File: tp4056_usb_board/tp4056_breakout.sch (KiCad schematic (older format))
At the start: 15 parts, among them J1 USB_OTG, J2 CONN_02X04, J3 DW01, J4 8205A, U1 TP4056_BREAKOUT

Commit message: Started the charging+UART breakout
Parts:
- C1, C2: footprint Capacitors_SMD:C_0805 -> Capacitors_SMD:C_0603
- D1, D2: footprint Diodes_SMD:D_0805 -> Diodes_SMD:D_0603
- J1: footprint (none) -> footprints:MICROUSB_SIMPLE
- R1, R2, R3, R4, R5: footprint Resistors_SMD:R_0805 -> Resistors_SMD:R_0603
- U1: footprint (none) -> tp4056_usb_board:TP4056_BREAKOUT
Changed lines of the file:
@@
 LIBS:valves
 LIBS:tp4056_breakout
+LIBS:tp4056_breakout-cache
 EELAYER 25 0
 EELAYER END
@@
 F 0 "C2" H 5775 2650 50  0000 L CNN
 F 1 "C" H 5775 2450 50  0000 L CNN
-F 2 "Capacitors_SMD:C_0805" H 5788 2400 50  0001 C CNN
+F 2 "Capacitors_SMD:C_0603" H 5788 2400 50  0001 C CNN
 F 3 "" H 5750 2550 50  0001 C CNN
 	1    5750 2550
@@
 F 0 "J1" H 3400 3000 50  0000 L CNN
 F 1 "USB_OTG" H 3400 2900 50  0000 L CNN
-F 2 "" H 3750 2500 50  0001 C CNN
+F 2 "footprints:MICROUSB_SIMPLE" H 3750 2500 50  0001 C CNN
 F 3 "" H 3750 2500 50  0001 C CNN
 	1    3600 2550
@@
 F 0 "R4" V 6480 2350 50  0000 C CNN
 F 1 "R" V 6400 2350 50  0000 C CNN
-F 2 "Resistors_SMD:R_0805" V 6330 2350 50  0001 C CNN
+F 2 "Resistors_SMD:R_0603" V 6330 2350 50  0001 C CNN
 F 3 "" H 6400 2350 50  0001 C CNN
 	1    6400 2350
@@
 F 0 "D2" H 5850 3900 50  0000 C CNN
 F 1 "LED" H 5850 3700 50  0000 C CNN
-F 2 "Diodes_SMD:D_0805" H 5850 3800 50  0001 C CNN
+F 2 "Diodes_SMD:D_0603" H 5850 3800 50  0001 C CNN
 F 3 "" H 5850 3800 50  0001 C CNN
 	1    5850 3800
@@
 F 0 "R3" V 5630 3800 50  0000 C CNN
 F 1 "R" V 5550 3800 50  0000 C CNN
-F 2 "Resistors_SMD:R_0805" V 5480 3800 50  0001 C CNN
+F 2 "Resistors_SMD:R_0603" V 5480 3800 50  0001 C CNN
 F 3 "" H 5550 3800 50  0001 C CNN
 	1    5550 3800
@@
 F 0 "D1" H 4450 4000 50  0000 C CNN
 F 1 "LED" H 4450 3800 50  0000 C CNN
-F 2 "Diodes_SMD:D_0805" H 4450 3900 50  0001 C CNN
+F 2 "Diodes_SMD:D_0603" H 4450 3900 50  0001 C CNN
 F 3 "" H 4450 3900 50  0001 C CNN
 	1    4450 3900
@@
 F 0 "R1" V 4650 3900 50  0000 C CNN
 F 1 "R" V 4750 3900 50  0000 C CNN
-F 2 "Resistors_SMD:R_0805" V 4680 3900 50  0001 C CNN
+F 2 "Resistors_SMD:R_0603" V 4680 3900 50  0001 C CNN
 F 3 "" H 4750 3900 50  0001 C CNN
 	1    4750 3900
@@
 $EndComp
 $Comp
-L VSS #PWR15
+L VSS #PWR01
 U 1 1 595C1537
 P 5750 2400
-F 0 "#PWR15" H 5750 2250 50  0001 C CNN
+F 0 "#PWR01" H 5750 2250 50  0001 C CNN
 F 1 "VSS" V 5750 2600 50  0000 C CNN
 F 2 "" H 5750 2400 50  0001 C CNN
@@
 NoConn ~ 3900 2750
 $Comp
-L GND #PWR1
+L GND #PWR02
 U 1 1 595C168E
 P 3500 2950
-F 0 "#PWR1" H 3500 2700 50  0001 C CNN
+F 0 "#PWR02" H 3500 2700 50  0001 C CNN
 F 1 "GND" H 3500 2800 50  0000 C CNN
 F 2 "" H 3500 2950 50  0001 C CNN
@@
 $EndComp
 $Comp
-L GND #PWR2
+L GND #PWR03
 U 1 1 595C16C7
 P 3600 2950
-F 0 "#PWR2" H 3600 2700 50  0001 C CNN
+F 0 "#PWR03" H 3600 2700 50  0001 C CNN
 F 1 "GND" H 3600 2800 50  0000 C CNN
 F 2 "" H 3600 2950 50  0001 C CNN
@@
 F 0 "C1" H 4825 3550 50  0000 L CNN
 F 1 "C" H 4825 3350 50  0000 L CNN
-F 2 "Capacitors_SMD:C_0805" H 4838 3300 50  0001 C CNN
+F 2 "Capacitors_SMD:C_0603" H 4838 3300 50  0001 C CNN
 F 3 "" H 4800 3450 50  0001 C CNN
 	1    4800 3450
@@
 F 0 "R2" V 5580 3450 50  0000 C CNN
 F 1 "R" V 5500 3450 50  0000 C CNN
-F 2 "Resistors_SMD:R_0805" V 5430 3450 50  0001 C CNN
+F 2 "Resistors_SMD:R_0603" V 5430 3450 50  0001 C CNN
 F 3 "" H 5500 3450 50  0001 C CNN
 	1    5500 3450
@@
 $EndComp
 $Comp
-L GND #PWR14
+L GND #PWR04
 U 1 1 595C1A34
 P 5500 3300
-F 0 "#PWR14" H 5500 3050 50  0001 C CNN
+F 0 "#PWR04" H 5500 3050 50  0001 C CNN
 F 1 "GND" H 5500 3150 50  0000 C CNN
 F 2 "" H 5500 3300 50  0001 C CNN
@@
 $EndComp
 $Comp
-L GND #PWR8
+L GND #PWR05
 U 1 1 595C1C7D
 P 4900 3700
-F 0 "#PWR8" H 4900 3450 50  0001 C CNN
+F 0 "#PWR05" H 4900 3450 50  0001 C CNN
 F 1 "GND" V 4850 3500 50  0000 C CNN
 F 2 "" H 4900 3700 50  0001 C CNN
@@
 $EndComp
 $Comp
-L +5V #PWR3
+L +5V #PWR06
 U 1 1 595C216B
 P 3900 2350
-F 0 "#PWR3" H 3900 2200 50  0001 C CNN
+F 0 "#PWR06" H 3900 2200 50  0001 C CNN
 F 1 "+5V" H 3900 2490 50  0000 C CNN
 F 2 "" H 3900 2350 50  0001 C CNN
@@
 $EndComp
 $Comp
-L +5V #PWR17
+L +5V #PWR07
 U 1 1 595C21FD
 P 6000 3800
-F 0 "#PWR17" H 6000 3650 50  0001 C CNN
+F 0 "#PWR07" H 6000 3650 50  0001 C CNN
 F 1 "+5V" H 6000 3940 50  0000 C CNN
 F 2 "" H 6000 3800 50  0001 C CNN
@@
 $EndComp
 $Comp
-L +5V #PWR12
+L +5V #PWR08
 U 1 1 595C2374
 P 5400 3700
-F 0 "#PWR12" H 5400 3550 50  0001 C CNN
+F 0 "#PWR08" H 5400 3550 50  0001 C CNN
 F 1 "+5V" V 5400 3900 50  0000 C CNN
 F 2 "" H 5400 3700 50  0001 C CNN
@@
 $EndComp
 $Comp
-L +5V #PWR7
+L +5V #PWR09
 U 1 1 595C23EE
 P 4800 3300
-F 0 "#PWR7" H 4800 3150 50  0001 C CNN
+F 0 "#PWR09" H 4800 3150 50  0001 C CNN
 F 1 "+5V" H 4800 3440 50  0000 C CNN
 F 2 "" H 4800 3300 50  0001 C CNN
@@
 $EndComp
 $Comp
-L +5V #PWR13
+L +5V #PWR010
 U 1 1 595C2423
 P 5400 3900
-F 0 "#PWR13" H 5400 3750 50  0001 C CNN
+F 0 "#PWR010" H 5400 3750 50  0001 C CNN
 F 1 "+5V" V 5500 4050 50  0000 C CNN
 F 2 "" H 5400 3900 50  0001 C CNN
@@
 $EndComp
 $Comp
-L +5V #PWR4
+L +5V #PWR011
 U 1 1 595C271A
 P 4300 3900
-F 0 "#PWR4" H 4300 3750 50  0001 C CNN
+F 0 "#PWR011" H 4300 3750 50  0001 C CNN
 F 1 "+5V" H 4300 4040 50  0000 C CNN
 F 2 "" H 4300 3900 50  0001 C CNN
@@
 $EndComp
 $Comp
-L GND #PWR16
+L GND #PWR012
 U 1 1 595C274F
 P 5750 2700
-F 0 "#PWR16" H 5750 2450 50  0001 C CNN
+F 0 "#PWR012" H 5750 2450 50  0001 C CNN
 F 1 "GND" V 5700 2500 50  0000 C CNN
 F 2 "" H 5750 2700 50  0001 C CNN
@@
 $EndComp
 $Comp
-L VSS #PWR9
+L VSS #PWR013
 U 1 1 595C2784
 P 4900 3800
-F 0 "#PWR9" H 4900 3650 50  0001 C CNN
+F 0 "#PWR013" H 4900 3650 50  0001 C CNN
 F 1 "VSS" V 4900 4000 50  0000 C CNN
 F 2 "" H 4900 3800 50  0001 C CNN
@@
 $EndComp
 $Comp
-L VSS #PWR18
+L VSS #PWR014
 U 1 1 595C27B9
 P 6400 2200
-F 0 "#PWR18" H 6400 2050 50  0001 C CNN
+F 0 "#PWR014" H 6400 2050 50  0001 C CNN
 F 1 "VSS" V 6400 2400 50  0000 C CNN
 F 2 "" H 6400 2200 50  0001 C CNN
@@
 $EndComp
 $Comp
-L GND #PWR19
+L GND #PWR015
 U 1 1 595C27EE
 P 7350 2900
-F 0 "#PWR19" H 7350 2650 50  0001 C CNN
+F 0 "#PWR015" H 7350 2650 50  0001 C CNN
 F 1 "GND" H 7350 2750 50  0000 C CNN
 F 2 "" H 7350 2900 50  0001 C CNN
@@
 	6950 3200 6950 3350
 $Comp
-L GND #PWR20
+L GND #PWR016
 U 1 1 595C2A57
 P 6950 3900
-F 0 "#PWR20" H 6950 3650 50  0001 C CNN
+F 0 "#PWR016" H 6950 3650 50  0001 C CNN
 F 1 "GND" V 6900 3700 50  0000 C CNN
 F 2 "" H 6950 3900 50  0001 C CNN
@@
 F 0 "U1" H 4600 2300 60  0000 C CNN
 F 1 "TP4056_BREAKOUT" H 4900 2800 60  0000 C CNN
-F 2 "" H 4800 2550 60  0001 C CNN
+F 2 "tp4056_usb_board:TP4056_BREAKOUT" H 4800 2550 60  0001 C CNN
 F 3 "" H 4800 2550 60  0001 C CNN
 	1    4800 2550
@@
 $EndComp
 $Comp
-L +5V #PWR10
+L +5V #PWR017
 U 1 1 595C2D30
 P 5250 2500
-F 0 "#PWR10" H 5250 2350 50  0001 C CNN
+F 0 "#PWR017" H 5250 2350 50  0001 C CNN
 F 1 "+5V" H 5250 2640 50  0000 C CNN
 F 2 "" H 5250 2500 50  0001 C CNN
@@
 $EndComp
 $Comp
-L GND #PWR11
+L GND #PWR018
 U 1 1 595C2D68
 P 5250 2600
-F 0 "#PWR11" H 5250 2350 50  0001 C CNN
+F 0 "#PWR018" H 5250 2350 50  0001 C CNN
 F 1 "GND" V 5200 2400 50  0000 C CNN
 F 2 "" H 5250 2600 50  0001 C CNN
@@
 $EndComp
 $Comp
-L GND #PWR6
+L GND #PWR019
 U 1 1 595C2DA0
 P 4350 2700
-F 0 "#PWR6" H 4350 2450 50  0001 C CNN
+F 0 "#PWR019" H 4350 2450 50  0001 C CNN
 F 1 "GND" V 4300 2500 50  0000 C CNN
 F 2 "" H 4350 2700 50  0001 C CNN
@@
 	4350 2400 4350 2500
 $Comp
-L VSS #PWR5
+L VSS #PWR020
 U 1 1 595C2E3E
 P 4350 2400
-F 0 "#PWR5" H 4350 2250 50  0001 C CNN
+F 0 "#PWR020" H 4350 2250 50  0001 C CNN
 F 1 "VSS" V 4350 2600 50  0000 C CNN
 F 2 "" H 4350 2400 50  0001 C CNN
@@
 F 0 "R5" V 7280 2900 50  0000 C CNN
 F 1 "R" V 7200 2900 50  0000 C CNN
-F 2 "Resistors_SMD:R_0805" V 7130 2900 50  0001 C CNN
+F 2 "Resistors_SMD:R_0603" V 7130 2900 50  0001 C CNN
 F 3 "" H 7200 2900 50  0001 C CNN
 	1    7200 2900

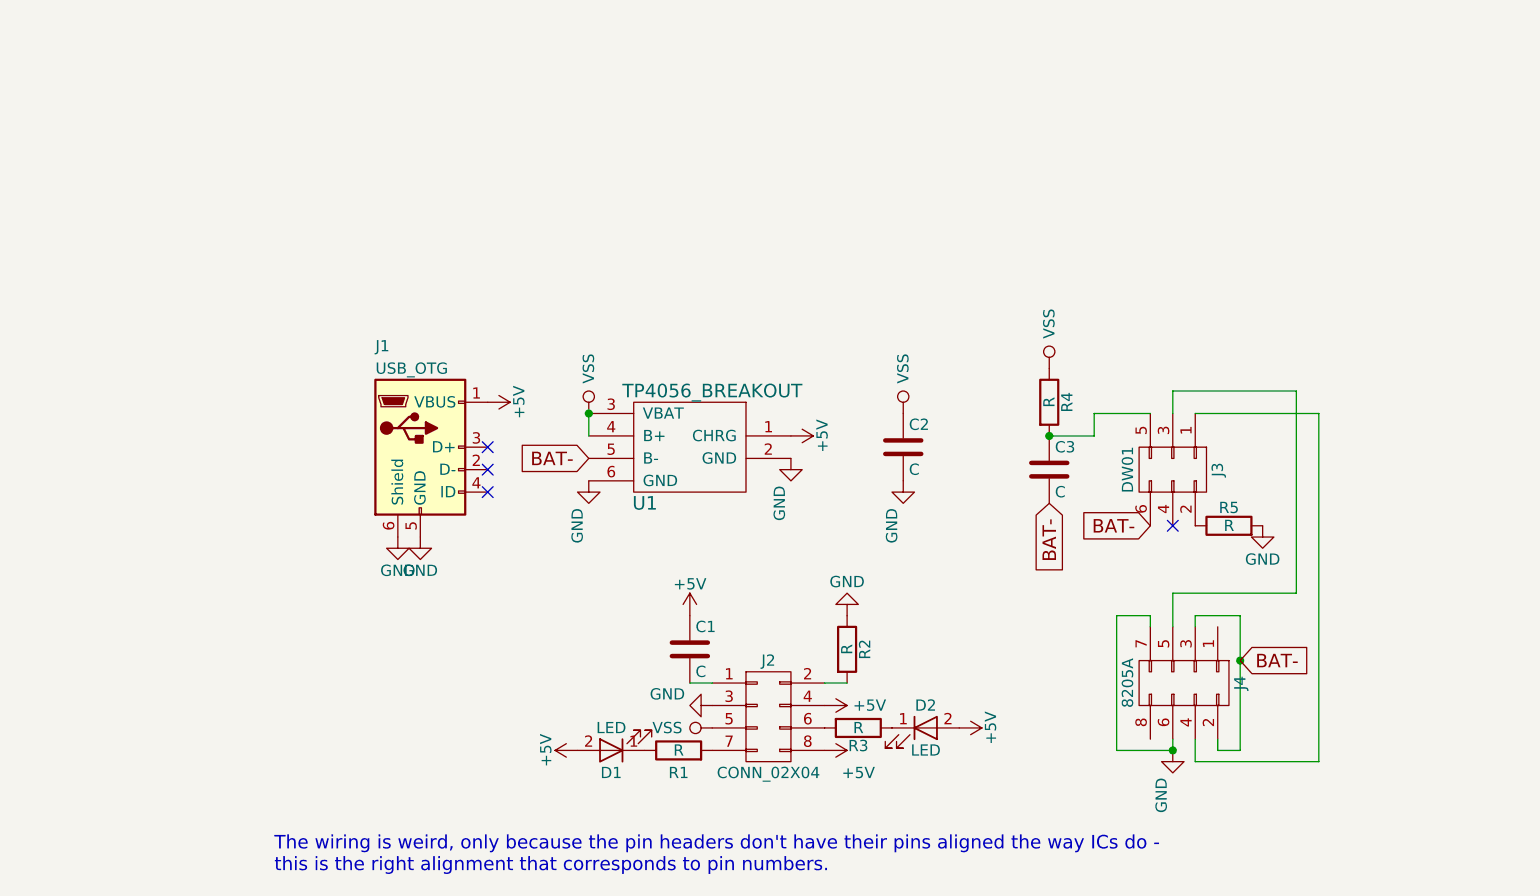
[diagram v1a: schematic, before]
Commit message: TP4056+UART board almost ready
-Figure out UART castellation placement & add traces to there
-Add thermal vias & mask openings
-Check pads on corners - convert to rectangle pads & enlarge holes
-Verify everything once again against the original boards
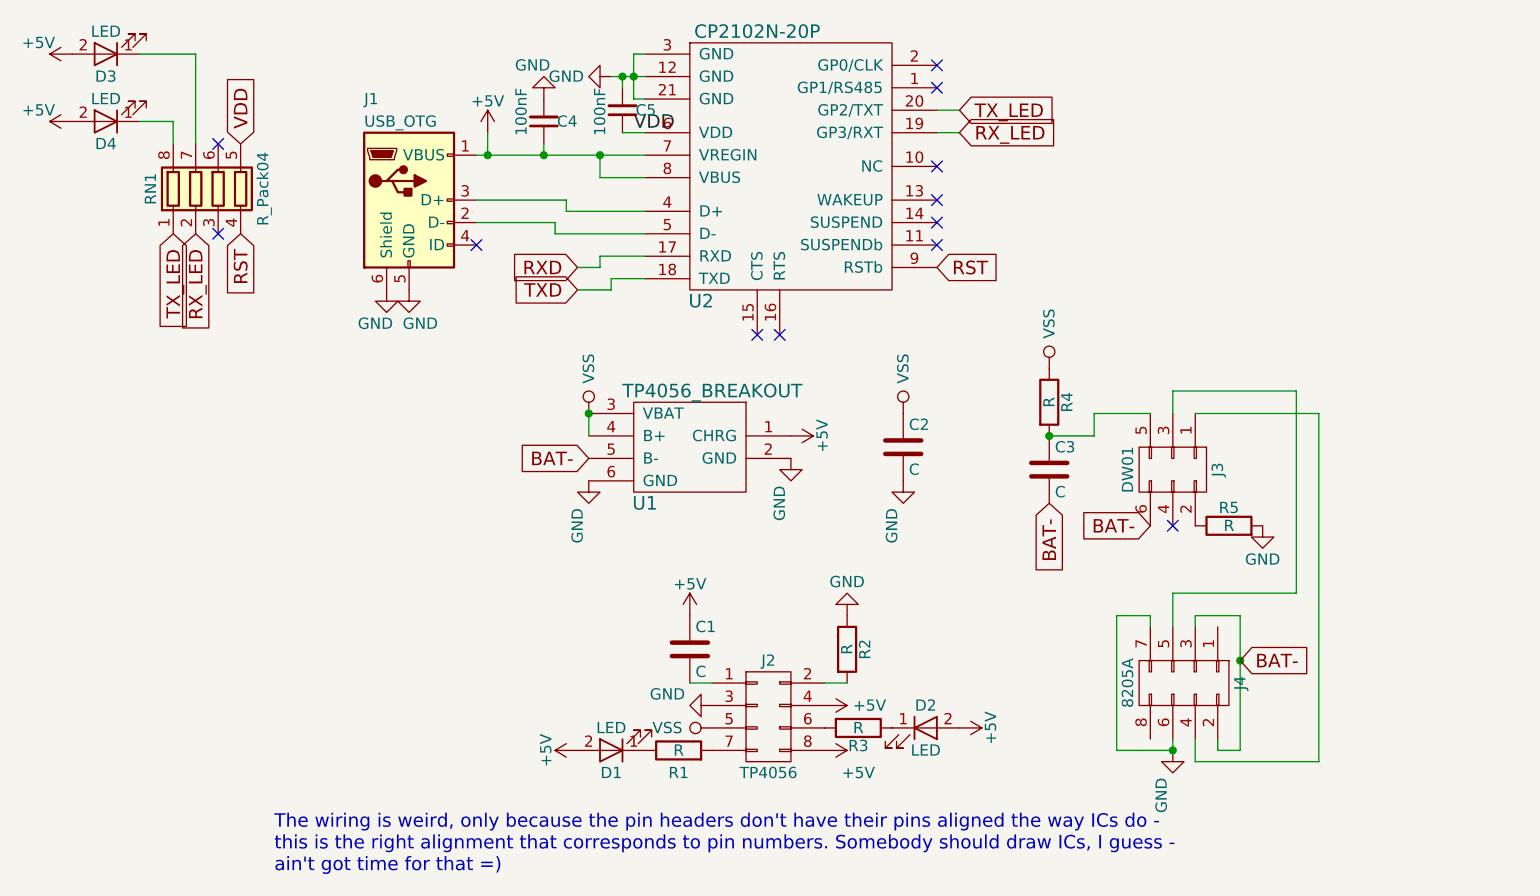
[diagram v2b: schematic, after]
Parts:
- added C4, C5: 100nF, Capacitors_SMD:C_0603, symbol C_Small
- added D3, D4: LED, Diodes_SMD:D_0603, symbol LED
- added RN1: R_Pack04, Resistors_SMD:R_Array_Concave_4x0402, symbol R_Pack04
- added U2: CP2102N-20P, CP2102N_QFN20:QFN-20-1EP_3x3mm_Pitch0.5, symbol CP2102N-20P
- J2: value CONN_02X04 -> TP4056
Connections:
- net +5V: now also C4.1, D3.2 (A), D4.2 (A), U2.7 (VREGIN), U2.8 (VBUS)
- net GND: now also C4.2, C5.2, U2.12 (GND), U2.21 (GND), U2.3 (GND)
- net at J1.2 (D-): now also U2.5 (D-)
- net at J1.3 (D+): now also U2.4 (D+)
- new net: D3.1 (K), RN1.7 (R2.2)
- new net: D4.1 (K), RN1.8 (R1.2)
- new net RST: RN1.4 (R4.1), U2.9 (RSTb)
- new net RXD: U2.17 (RXD)
- new net RX_LED: RN1.2 (R2.1), U2.19 (GP3/RXT)
- new net TXD: U2.18 (TXD)
- new net TX_LED: RN1.1 (R1.1), U2.20 (GP2/TXT)
- new net VDD: C5.1, RN1.5 (R4.2), U2.6 (VDD)
- no-connect marks 4 -> 12
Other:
- note added: "The wiring is weird, only because the pin headers don't have their pins aligned the way ICs do - \nthis is the right alignment that corresponds to pin numbers. Somebody should draw ICs, I guess - \nain't got time for that =)\n"
- note removed: "The wiring is weird, only because the pin headers don't have their pins aligned the way ICs do - \nthis is the right alignment that corresponds to pin numbers."
- moved on the sheet: J1

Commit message: Finished TP4056 charging+USB-UART board
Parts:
- added J5: TEST_2P, Pin_Headers:Pin_Header_Straight_1x02_Pitch2.00mm, symbol TEST_2P
- D1, D2, D3, D4: footprint Diodes_SMD:D_0603 -> Resistors_SMD:R_0603_HandSoldering
- U2: symbol CP2102N-20P -> CP2102N-20P-RESCUE-tp4056_breakout
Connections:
- net RXD: now also J5.1
- net TXD: now also J5.2
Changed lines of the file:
@@
 EESchema Schematic File Version 2
+LIBS:tp4056_breakout-rescue
 LIBS:power
 LIBS:device
@@
 F 0 "D2" H 5850 3900 50  0000 C CNN
 F 1 "LED" H 5850 3700 50  0000 C CNN
-F 2 "Diodes_SMD:D_0603" H 5850 3800 50  0001 C CNN
+F 2 "Resistors_SMD:R_0603_HandSoldering" H 5850 3800 50  0001 C CNN
 F 3 "" H 5850 3800 50  0001 C CNN
 	1    5850 3800
@@
 F 0 "D1" H 4450 4000 50  0000 C CNN
 F 1 "LED" H 4450 3800 50  0000 C CNN
-F 2 "Diodes_SMD:D_0603" H 4450 3900 50  0001 C CNN
+F 2 "Resistors_SMD:R_0603_HandSoldering" H 4450 3900 50  0001 C CNN
 F 3 "" H 4450 3900 50  0001 C CNN
 	1    4450 3900
@@
 $EndComp
 $Comp
-L VSS #PWR01
+L VSS #PWR19
 U 1 1 595C1537
 P 5750 2400
-F 0 "#PWR01" H 5750 2250 50  0001 C CNN
+F 0 "#PWR19" H 5750 2250 50  0001 C CNN
 F 1 "VSS" V 5750 2600 50  0000 C CNN
 F 2 "" H 5750 2400 50  0001 C CNN
@@
 NoConn ~ 3850 1650
 $Comp
-L GND #PWR02
+L GND #PWR3
 U 1 1 595C168E
 P 3450 1850
-F 0 "#PWR02" H 3450 1600 50  0001 C CNN
+F 0 "#PWR3" H 3450 1600 50  0001 C CNN
 F 1 "GND" H 3400 1700 50  0000 C CNN
 F 2 "" H 3450 1850 50  0001 C CNN
@@
 $EndComp
 $Comp
-L GND #PWR03
+L GND #PWR4
 U 1 1 595C16C7
 P 3550 1850
-F 0 "#PWR03" H 3550 1600 50  0001 C CNN
+F 0 "#PWR4" H 3550 1600 50  0001 C CNN
 F 1 "GND" H 3600 1700 50  0000 C CNN
 F 2 "" H 3550 1850 50  0001 C CNN
@@
 $EndComp
 $Comp
-L GND #PWR04
+L GND #PWR18
 U 1 1 595C1A34
 P 5500 3300
-F 0 "#PWR04" H 5500 3050 50  0001 C CNN
+F 0 "#PWR18" H 5500 3050 50  0001 C CNN
 F 1 "GND" H 5500 3150 50  0000 C CNN
 F 2 "" H 5500 3300 50  0001 C CNN
@@
 $EndComp
 $Comp
-L GND #PWR05
+L GND #PWR12
 U 1 1 595C1C7D
 P 4900 3700
-F 0 "#PWR05" H 4900 3450 50  0001 C CNN
+F 0 "#PWR12" H 4900 3450 50  0001 C CNN
 F 1 "GND" V 4850 3500 50  0000 C CNN
 F 2 "" H 4900 3700 50  0001 C CNN
@@
 $EndComp
 $Comp
-L +5V #PWR06
+L +5V #PWR5
 U 1 1 595C216B
 P 3900 1150
-F 0 "#PWR06" H 3900 1000 50  0001 C CNN
+F 0 "#PWR5" H 3900 1000 50  0001 C CNN
 F 1 "+5V" H 3900 1290 50  0000 C CNN
 F 2 "" H 3900 1150 50  0001 C CNN
@@
 $EndComp
 $Comp
-L +5V #PWR07
+L +5V #PWR21
 U 1 1 595C21FD
 P 6000 3800
-F 0 "#PWR07" H 6000 3650 50  0001 C CNN
+F 0 "#PWR21" H 6000 3650 50  0001 C CNN
 F 1 "+5V" H 6000 3940 50  0000 C CNN
 F 2 "" H 6000 3800 50  0001 C CNN
@@
 $EndComp
 $Comp
-L +5V #PWR08
+L +5V #PWR16
 U 1 1 595C2374
 P 5400 3700
-F 0 "#PWR08" H 5400 3550 50  0001 C CNN
+F 0 "#PWR16" H 5400 3550 50  0001 C CNN
 F 1 "+5V" V 5400 3900 50  0000 C CNN
 F 2 "" H 5400 3700 50  0001 C CNN
@@
 $EndComp
 $Comp
-L +5V #PWR09
+L +5V #PWR11
 U 1 1 595C23EE
 P 4800 3300
-F 0 "#PWR09" H 4800 3150 50  0001 C CNN
+F 0 "#PWR11" H 4800 3150 50  0001 C CNN
 F 1 "+5V" H 4800 3440 50  0000 C CNN
 F 2 "" H 4800 3300 50  0001 C CNN
@@
 $EndComp
 $Comp
-L +5V #PWR010
+L +5V #PWR17
 U 1 1 595C2423
 P 5400 3900
-F 0 "#PWR010" H 5400 3750 50  0001 C CNN
+F 0 "#PWR17" H 5400 3750 50  0001 C CNN
 F 1 "+5V" V 5500 4050 50  0000 C CNN
 F 2 "" H 5400 3900 50  0001 C CNN
@@
 $EndComp
 $Comp
-L +5V #PWR011
+L +5V #PWR7
 U 1 1 595C271A
 P 4300 3900
-F 0 "#PWR011" H 4300 3750 50  0001 C CNN
+F 0 "#PWR7" H 4300 3750 50  0001 C CNN
 F 1 "+5V" H 4300 4040 50  0000 C CNN
 F 2 "" H 4300 3900 50  0001 C CNN
@@
 $EndComp
 $Comp
-L GND #PWR012
+L GND #PWR20
 U 1 1 595C274F
 P 5750 2700
-F 0 "#PWR012" H 5750 2450 50  0001 C CNN
+F 0 "#PWR20" H 5750 2450 50  0001 C CNN
 F 1 "GND" V 5700 2500 50  0000 C CNN
 F 2 "" H 5750 2700 50  0001 C CNN
@@
 $EndComp
 $Comp
-L VSS #PWR013
+L VSS #PWR13
 U 1 1 595C2784
 P 4900 3800
-F 0 "#PWR013" H 4900 3650 50  0001 C CNN
+F 0 "#PWR13" H 4900 3650 50  0001 C CNN
 F 1 "VSS" V 4900 4000 50  0000 C CNN
 F 2 "" H 4900 3800 50  0001 C CNN
@@
 $EndComp
 $Comp
-L VSS #PWR014
+L VSS #PWR22
 U 1 1 595C27B9
 P 6400 2200
-F 0 "#PWR014" H 6400 2050 50  0001 C CNN
+F 0 "#PWR22" H 6400 2050 50  0001 C CNN
 F 1 "VSS" V 6400 2400 50  0000 C CNN
 F 2 "" H 6400 2200 50  0001 C CNN
@@
 $EndComp
 $Comp
-L GND #PWR015
+L GND #PWR24
 U 1 1 595C27EE
 P 7350 2900
-F 0 "#PWR015" H 7350 2650 50  0001 C CNN
+F 0 "#PWR24" H 7350 2650 50  0001 C CNN
 F 1 "GND" H 7350 2750 50  0000 C CNN
 F 2 "" H 7350 2900 50  0001 C CNN
@@
 $EndComp
 $Comp
-L GND #PWR016
+L GND #PWR23
 U 1 1 595C2A57
 P 6950 3900
-F 0 "#PWR016" H 6950 3650 50  0001 C CNN
+F 0 "#PWR23" H 6950 3650 50  0001 C CNN
 F 1 "GND" V 6900 3700 50  0000 C CNN
 F 2 "" H 6950 3900 50  0001 C CNN
@@
 $EndComp
 $Comp
-L +5V #PWR017
+L +5V #PWR14
 U 1 1 595C2D30
 P 5250 2500
-F 0 "#PWR017" H 5250 2350 50  0001 C CNN
+F 0 "#PWR14" H 5250 2350 50  0001 C CNN
 F 1 "+5V" H 5250 2640 50  0000 C CNN
 F 2 "" H 5250 2500 50  0001 C CNN
@@
 $EndComp
 $Comp
-L GND #PWR018
+L GND #PWR15
 U 1 1 595C2D68
 P 5250 2600
-F 0 "#PWR018" H 5250 2350 50  0001 C CNN
+F 0 "#PWR15" H 5250 2350 50  0001 C CNN
 F 1 "GND" V 5200 2400 50  0000 C CNN
 F 2 "" H 5250 2600 50  0001 C CNN
@@
 $EndComp
 $Comp
-L GND #PWR019
+L GND #PWR9
 U 1 1 595C2DA0
 P 4350 2700
-F 0 "#PWR019" H 4350 2450 50  0001 C CNN
+F 0 "#PWR9" H 4350 2450 50  0001 C CNN
 F 1 "GND" V 4300 2500 50  0000 C CNN
 F 2 "" H 4350 2700 50  0001 C CNN
@@
 $EndComp
 $Comp
-L VSS #PWR020
+L VSS #PWR8
 U 1 1 595C2E3E
 P 4350 2400
-F 0 "#PWR020" H 4350 2250 50  0001 C CNN
+F 0 "#PWR8" H 4350 2250 50  0001 C CNN
 F 1 "VSS" V 4350 2600 50  0000 C CNN
 F 2 "" H 4350 2400 50  0001 C CNN
@@
 BAT-
 $Comp
-L GND #PWR021
+L GND #PWR10
 U 1 1 59A5E3A9
 P 4450 900
-F 0 "#PWR021" H 4450 650 50  0001 C CNN
+F 0 "#PWR10" H 4450 650 50  0001 C CNN
 F 1 "GND" V 4450 700 50  0000 C CNN
 F 2 "" H 4450 900 50  0001 C CNN
@@
 Connection ~ 3900 1250
 $Comp
-L GND #PWR022
+L GND #PWR6
 U 1 1 59A5FF0F
 P 4150 1000
-F 0 "#PWR022" H 4150 750 50  0001 C CNN
+F 0 "#PWR6" H 4150 750 50  0001 C CNN
 F 1 "GND" H 4200 850 50  0000 C CNN
 F 2 "" H 4150 1000 50  0001 C CNN
@@
 TX_LED
 $Comp
-L CP2102N-20P U2
+L CP2102N-20P-RESCUE-tp4056_breakout U2
 U 1 1 59A5DDC3
 P 5200 1350
@@
 F 0 "D4" H 2200 1200 50  0000 C CNN
 F 1 "LED" H 2200 1000 50  0000 C CNN
-F 2 "Diodes_SMD:D_0603" H 2200 1100 50  0001 C CNN
+F 2 "Resistors_SMD:R_0603_HandSoldering" H 2200 1100 50  0001 C CNN
 F 3 "" H 2200 1100 50  0001 C CNN
 	1    2200 1100
@@
 F 0 "D3" H 2200 900 50  0000 C CNN
 F 1 "LED" H 2200 700 50  0000 C CNN
-F 2 "Diodes_SMD:D_0603" H 2200 800 50  0001 C CNN
+F 2 "Resistors_SMD:R_0603_HandSoldering" H 2200 800 50  0001 C CNN
 F 3 "" H 2200 800 50  0001 C CNN
 	1    2200 800
@@
 	2500 1100 2500 1200
 $Comp
-L +5V #PWR023
+L +5V #PWR1
 U 1 1 59A6093E
 P 2050 800
-F 0 "#PWR023" H 2050 650 50  0001 C CNN
+F 0 "#PWR1" H 2050 650 50  0001 C CNN
 F 1 "+5V" V 2100 950 50  0000 C CNN
 F 2 "" H 2050 800 50  0001 C CNN
@@
 $EndComp
 $Comp
-L +5V #PWR024
+L +5V #PWR2
 U 1 1 59A609D1
 P 2050 1100
-F 0 "#PWR024" H 2050 950 50  0001 C CNN
+F 0 "#PWR2" H 2050 950 50  0001 C CNN
 F 1 "+5V" V 2100 1250 50  0000 C CNN
 F 2 "" H 2050 1100 50  0001 C CNN
@@
 NoConn ~ 2700 1200
 NoConn ~ 2700 1600
+$Comp
+L TEST_2P J5
+U 1 1 59A87ED6
+P 3150 2450
+F 0 "J5" H 3150 2510 50  0000 C CNN
+F 1 "TEST_2P" H 3150 2380 50  0000 C CNN
+F 2 "Pin_Headers:Pin_Header_Straight_1x02_Pitch2.00mm" H 3150 2450 50  0001 C CNN
+F 3 "" H 3150 2450 50  0001 C CNN
+	1    3150 2450
+	1    0    0    -1
+$EndComp
+Text GLabel 2950 2450 0    60   Input ~ 0
+RXD
+Text GLabel 3350 2450 2    60   Input ~ 0
+TXD
 $EndSCHEMATC
